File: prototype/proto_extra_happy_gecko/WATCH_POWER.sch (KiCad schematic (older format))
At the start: 11 parts

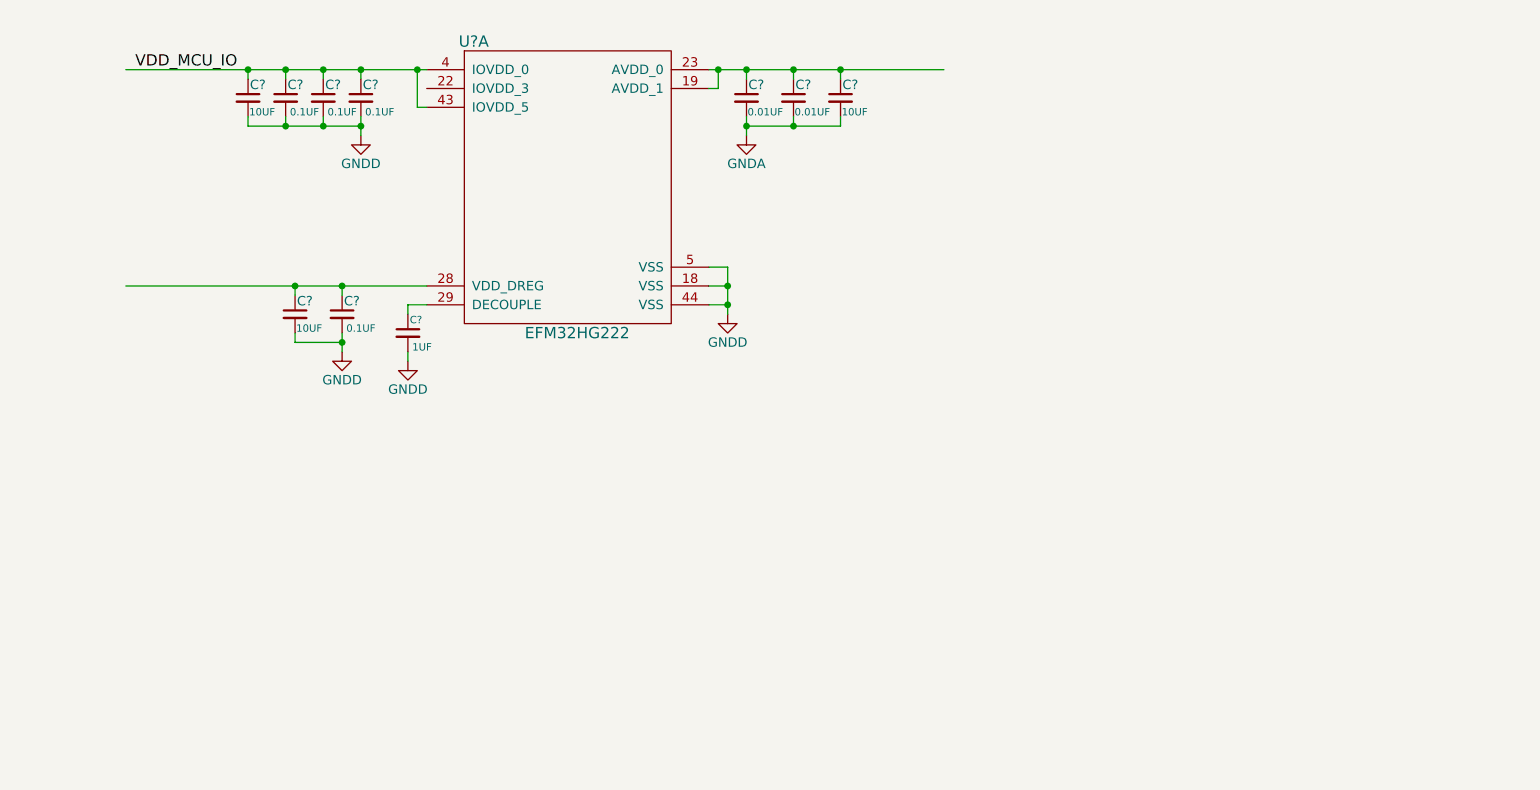
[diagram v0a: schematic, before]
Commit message: Added all leds, 3.3Vreg, and routed busses
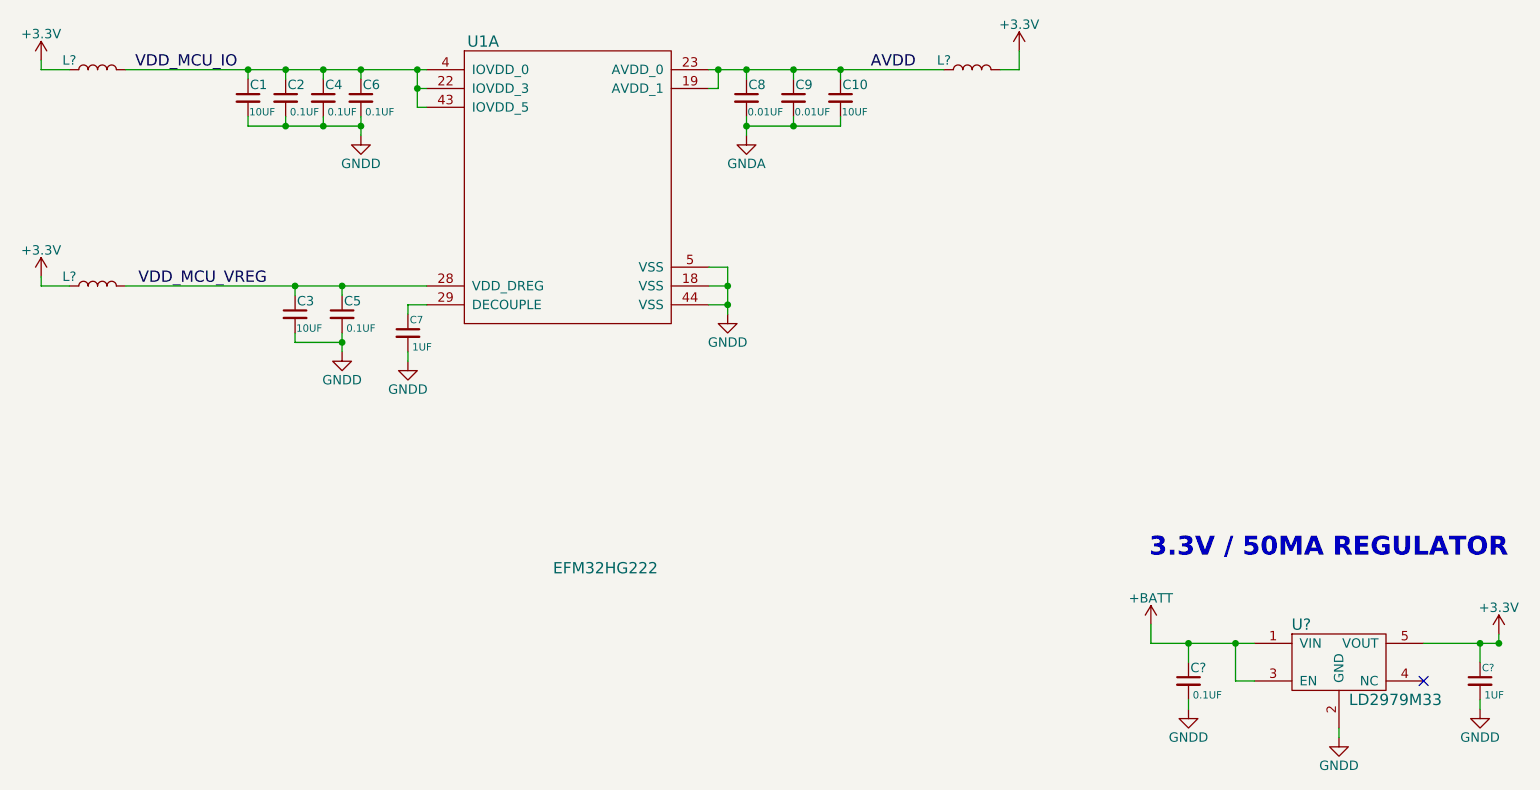
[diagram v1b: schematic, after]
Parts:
- removed U?: EFM32HG222, symbol EFM32HG222
- added C?: CAP_1UF_0402, symbol CAP_1UF_0402
- added C?: CAP_0.1UF_0402, symbol CAP_0.1UF_0402
- added L? (x3): EMI_FILTER_100MA, symbol EMI_FILTER_100MA
- added U1: EFM32HG222, symbol EFM32HG222
- added U?: LD2979M33, symbol LD2979M33
- gave numbers to parts that had none: 10
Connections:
- net labels added: +3.3V, +BATT, AVDD, VDD_MCU_VREG
- wire segments 35 -> 53
- no-connect marks 0 -> 1
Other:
- note added: "3.3V / 50MA REGULATOR"
